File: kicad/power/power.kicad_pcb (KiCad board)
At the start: 2 copper layers, 73 x 25.1 mm, 45 parts, among them J1 Conn_01x06, J2 Conn_01x09_Male, U1 LF353DR, U2 LF353DR, U3 LF353DR, U4 LM339DR, U5 LM339DR

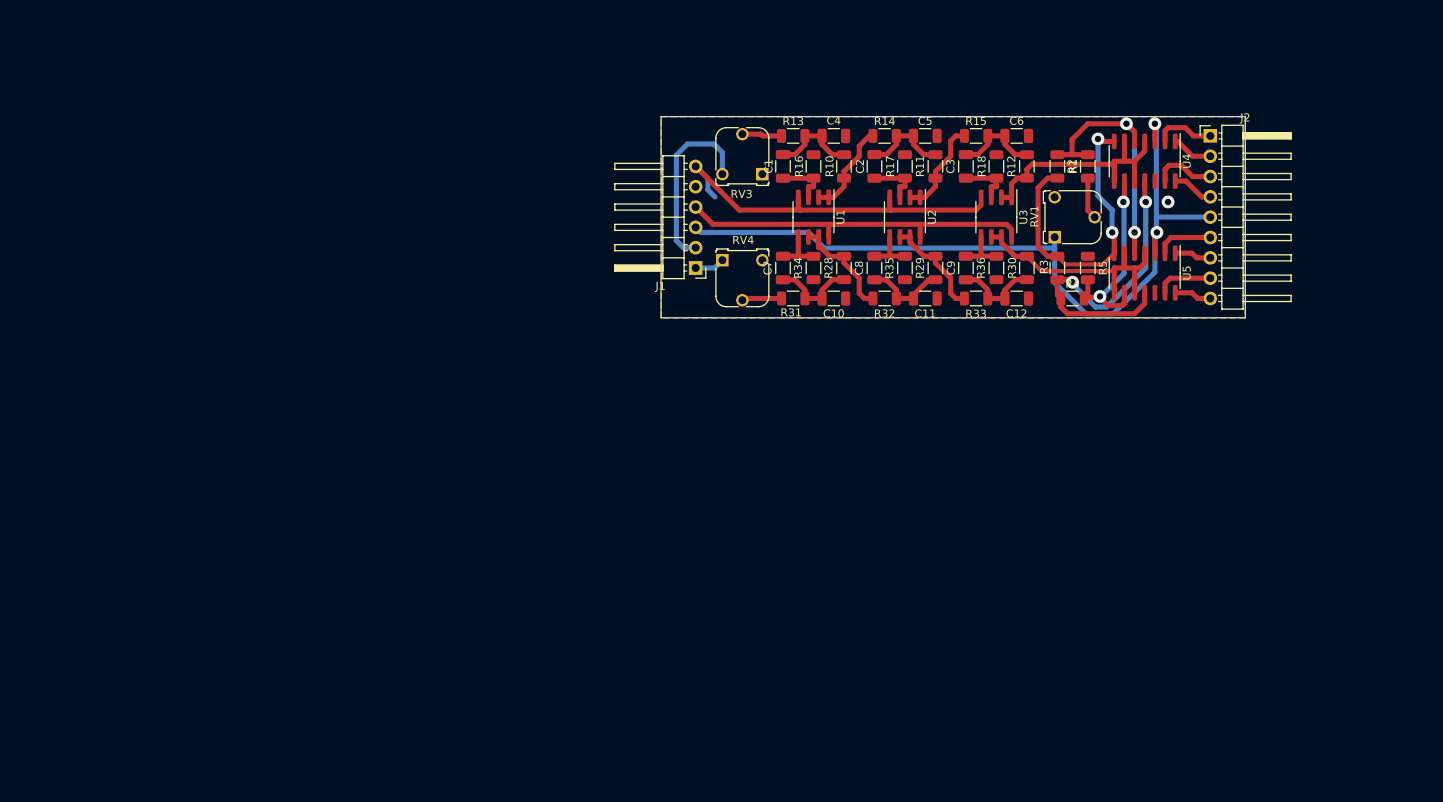
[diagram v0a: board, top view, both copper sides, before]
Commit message: Power schematic to pcb update
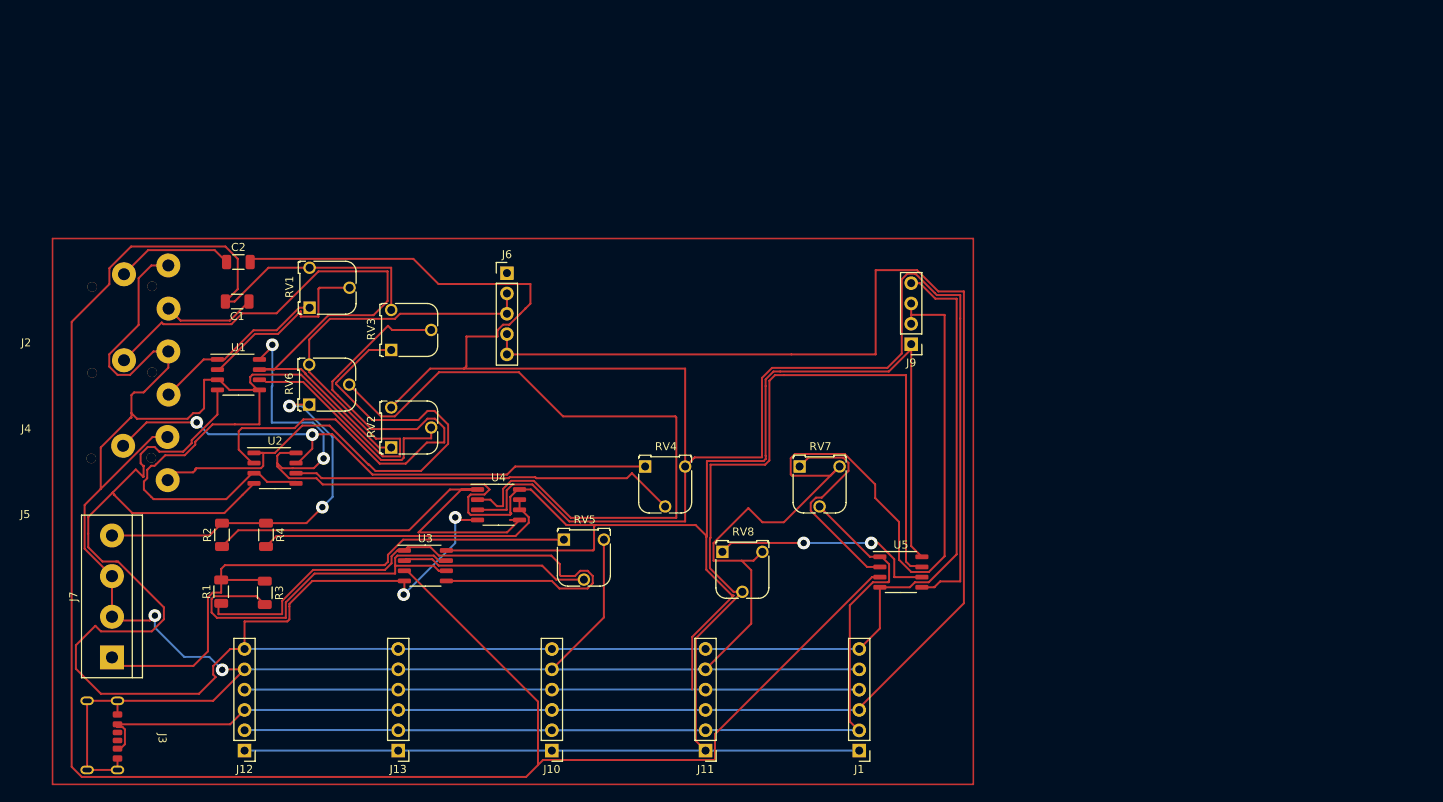
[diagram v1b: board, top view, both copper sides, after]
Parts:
- removed C10, C11, C12, C3, C4, C5, C6, C7, C8, C9: 100n, Capacitor_SMD:C_1206_3216Metric
- removed R10, R11, R12, R28, R29, R30: 137, Resistor_SMD:R_1206_3216Metric
- removed R13, R14, R15, R31, R32, R33: 931, Resistor_SMD:R_1206_3216Metric
- removed R16, R17, R18, R34, R35, R36: 1k87, Resistor_SMD:R_1206_3216Metric
- removed R5: 100k, Resistor_SMD:R_1206_3216Metric
- added J10: Conn_01x06, Connector_PinHeader_2.54mm:PinHeader_1x06_P2.54mm_Vertical, F.Cu at (103.2, 141.0)
- added J11: Conn_01x06, Connector_PinHeader_2.54mm:PinHeader_1x06_P2.54mm_Vertical, F.Cu at (122.4, 141.0)
- added J12: Conn_01x06, Connector_PinHeader_2.54mm:PinHeader_1x06_P2.54mm_Vertical, F.Cu at (64.8, 141.0)
- added J13: Conn_01x06, Connector_PinHeader_2.54mm:PinHeader_1x06_P2.54mm_Vertical, F.Cu at (84.0, 141.0)
- added J3: USB_C_Receptacle, audio_footprint:usb_footprint, F.Cu at (48.9, 139.4)
- added J4: AudioJack3, audio_footprint:audio_jack, F.Cu at (37.5, 101.2)
- added J5: AudioJack3, audio_footprint:audio_jack, F.Cu at (37.4, 111.9)
- added J6: Conn_01x05_Male, Connector_PinHeader_2.54mm:PinHeader_1x05_P2.54mm_Vertical, F.Cu at (97.6, 81.3)
- added J7: Screw_Terminal_01x02, TerminalBlock:TerminalBlock_bornier-4_P5.08mm, F.Cu at (48.2, 129.3)
- added J9: Conn_01x04_Male, Connector_PinHeader_2.54mm:PinHeader_1x04_P2.54mm_Vertical, F.Cu at (148.1, 90.2)
- added RV2: R_Potentiometer, Potentiometer_THT:Potentiometer_Runtron_RM-065_Vertical, F.Cu at (83.1, 103.1)
- added RV5: R_Potentiometer, Potentiometer_THT:Potentiometer_Runtron_RM-065_Vertical, F.Cu at (104.7, 114.6)
- added RV6: R_Potentiometer, Potentiometer_THT:Potentiometer_Runtron_RM-065_Vertical, F.Cu at (72.8, 97.7)
- added RV7: 2k2, Potentiometer_THT:Potentiometer_Runtron_RM-065_Vertical, F.Cu at (134.2, 105.5)
- added RV8: 2k2, Potentiometer_THT:Potentiometer_Runtron_RM-065_Vertical, F.Cu at (124.5, 116.1)
- C1, C2: value 100n -> C
- J1: footprint Connector_PinHeader_2.54mm:PinHeader_1x06_P2.54mm_Horizontal -> Connector_PinHeader_2.54mm:PinHeader_1x06_P2.54mm_Vertical
- J2: value Conn_01x09_Male -> AudioJack3; footprint Connector_PinHeader_2.54mm:PinHeader_1x09_P2.54mm_Horizontal -> audio_footprint:audio_jack
- R1, R2, R3, R4: value 100k -> 20
- RV1, RV3, RV4: value 10k -> R_Potentiometer
- U1, U2, U3: value LF353DR -> LM4565F-GE2; footprint Package_SO:SOIC-8_3.9x4.9mm_P1.27mm -> Package_SO:SOP-8_3.9x4.9mm_P1.27mm
- U4: value LM339DR -> LM4565F-GE2; footprint Package_SO:SO-14_3.9x8.65mm_P1.27mm -> Package_SO:SOP-8_3.9x4.9mm_P1.27mm
- U5: value LM339DR -> LF353DR; footprint Package_SO:SO-14_3.9x8.65mm_P1.27mm -> Package_SO:SOP-8_3.9x4.9mm_P1.27mm
- moved J2 150.4 mm to (37.5, 90.5)
- moved R1 120.7 mm to (61.9, 121.1)
- moved R2 114.1 mm to (62.0, 114.0), turned to 90 degrees
- moved R3 107.1 mm to (67.3, 121.2)
- moved R4 105.1 mm to (67.5, 114.0), turned to -90 degrees
- moved RV1 93.6 mm to (72.9, 85.6)
- moved U4 91.5 mm to (96.5, 110.2), turned to 0 degrees
- moved U2 84.8 mm to (68.6, 105.7), turned to 0 degrees
- moved U3 83.6 mm to (87.4, 117.9), turned to 0 degrees
- moved C2 80.4 mm to (64.0, 79.9), turned to 0 degrees
- moved U1 74.5 mm to (64.0, 94.0), turned to 0 degrees
- moved C1 70.3 mm to (63.9, 84.8), turned to 180 degrees
- moved J1 63.7 mm to (141.6, 141.0)
- moved RV3 51.3 mm to (83.1, 90.9), turned to 90 degrees
- moved U5 48.2 mm to (146.8, 118.7), turned to 0 degrees
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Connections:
- C1 pad 1: Net-(C4-Pad1) -> Net-(C1-Pad1)
- C1 pad 2: Net-(C1-Pad2) -> audio_in_L
- C2 pad 1: Net-(C5-Pad1) -> Net-(C2-Pad1)
- C2 pad 2: Net-(C2-Pad2) -> audio_in_R
- J1 pad 1: Net-(J1-Pad1) -> audio_right
- J1 pad 2: Net-(J1-Pad2) -> audio_lefT
- J2 pad 4: Net-(U4-Pad14) -> (no net)
- J2 pad 5: +5V -> (no net)
- R1 pad 2: Net-(R1-Pad2) -> speaker_left
- R2 pad 1: Net-(R1-Pad2) -> Net-(R2-Pad1)
- R2 pad 2: Net-(R2-Pad2) -> speaker_right
- R3 pad 1: Net-(R2-Pad2) -> speaker_left
- R4 pad 1: Net-(R3-Pad2) -> speaker_right
- RV1 pad 1: +5V -> Net-(J4-PadT)
- RV1 pad 2: Net-(R1-Pad1) -> Net-(RV1-Pad2)
- RV1 pad 3: GND -> audio_in_L
- RV3 pad 1: GND -> Net-(J5-PadT)
- RV3 pad 2: audio_left -> Net-(RV3-Pad2)
- RV3 pad 3: Net-(J1-Pad2) -> audio_in_L
- RV4 pad 1: Net-(J1-Pad1) -> Net-(J5-PadR)
- RV4 pad 2: audio_right -> Net-(RV4-Pad2)
- RV4 pad 3: GND -> audio_in_R
- U1 pad 1: Net-(R10-Pad2) -> Net-(J4-PadT)
- U1 pad 2: Net-(R10-Pad2) -> Net-(RV1-Pad2)
- U1 pad 3: Net-(C1-Pad2) -> GND
- U1 pad 5: Net-(C7-Pad2) -> GND
- U1 pad 6: Net-(R28-Pad2) -> Net-(RV2-Pad2)
- U1 pad 7: Net-(R28-Pad2) -> Net-(J4-PadR)
- U2 pad 1: Net-(R11-Pad2) -> Net-(J5-PadT)
- U2 pad 2: Net-(R11-Pad2) -> Net-(RV3-Pad2)
- U2 pad 3: Net-(C2-Pad2) -> GND
- U2 pad 5: Net-(C8-Pad2) -> GND
- U2 pad 6: Net-(R29-Pad2) -> Net-(RV4-Pad2)
- U2 pad 7: Net-(R29-Pad2) -> Net-(J5-PadR)
- U3 pad 1: Net-(R12-Pad2) -> Net-(R1-Pad1)
- U3 pad 2: Net-(R12-Pad2) -> Net-(RV5-Pad2)
- U3 pad 3: Net-(C3-Pad2) -> audio_in_L
- U3 pad 5: Net-(C9-Pad2) -> Net-(R1-Pad1)
- U3 pad 6: Net-(R30-Pad2) -> Net-(R3-Pad2)
- U3 pad 7: Net-(R30-Pad2) -> Net-(R3-Pad2)
- U4 pad 1: Net-(U4-Pad1) -> Net-(R2-Pad1)
- U4 pad 2: Net-(U4-Pad2) -> Net-(RV6-Pad2)
- U4 pad 3: +5V -> audio_in_R
- U4 pad 4: Net-(R12-Pad2) -> -15V
- U4 pad 5: Net-(R1-Pad2) -> Net-(R2-Pad1)
- U4 pad 6: Net-(R12-Pad2) -> Net-(R4-Pad2)
- U4 pad 7: Net-(R2-Pad2) -> Net-(R4-Pad2)
- U4 pad 8: Net-(R12-Pad2) -> +15V
- U5 pad 1: Net-(U5-Pad1) -> audio_lefT
- U5 pad 2: Net-(U5-Pad2) -> Net-(RV7-Pad1)
- U5 pad 3: +5V -> audio_in_L
- U5 pad 4: Net-(R30-Pad2) -> -15V
- U5 pad 5: Net-(R1-Pad2) -> audio_in_R
- U5 pad 6: Net-(R30-Pad2) -> Net-(RV8-Pad1)
- U5 pad 7: Net-(R2-Pad2) -> audio_right
- U5 pad 8: Net-(R30-Pad2) -> +15V
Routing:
- net GND: track 0.00 -> 492.8 mm, vias 1 -> 7
- net audio_in_L: track 0.00 -> 261.3 mm
- net +15V: track 44.8 -> 296.4 mm, vias 0 -> 7
- net -15V: track 46.4 -> 287.2 mm, vias 0 -> 7
- net audio_in_R: track 0.00 -> 239.6 mm
- net audio_right: track 4.98 -> 179.9 mm, vias 0 -> 4
- net +5V: track 98.4 -> 227.9 mm, vias 2 -> 5
- net audio_lefT: track 0.00 -> 113.0 mm, vias 0 -> 5
- net Net-(RV6-Pad2): track 0.00 -> 89.4 mm
- net Net-(J4-PadR): track 0.00 -> 81.6 mm
- net speaker_left: track 0.00 -> 75.2 mm
- net Net-(J5-PadR): track 0.00 -> 74.2 mm, vias 0 -> 2
- net Net-(J5-PadT): track 0.00 -> 73.2 mm
- net Net-(R1-Pad1): track 5.24 -> 76.0 mm
- net Net-(RV3-Pad2): track 0.00 -> 69.9 mm
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- removed copper zone on B.Cu, net GND
- removed copper zone on F.Cu, net GND
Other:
- board outline removed

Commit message: Did some stuff
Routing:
- net audio_in_R: track 239.6 -> 245.0 mm
- net -15V: track 287.2 -> 283.8 mm
- net GND: track 492.8 -> 491.9 mm
- added copper zone on B.Cu, net GND
- added copper zone on F.Cu, net GND
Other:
- board outline added: 115.3 x 68.1 mm

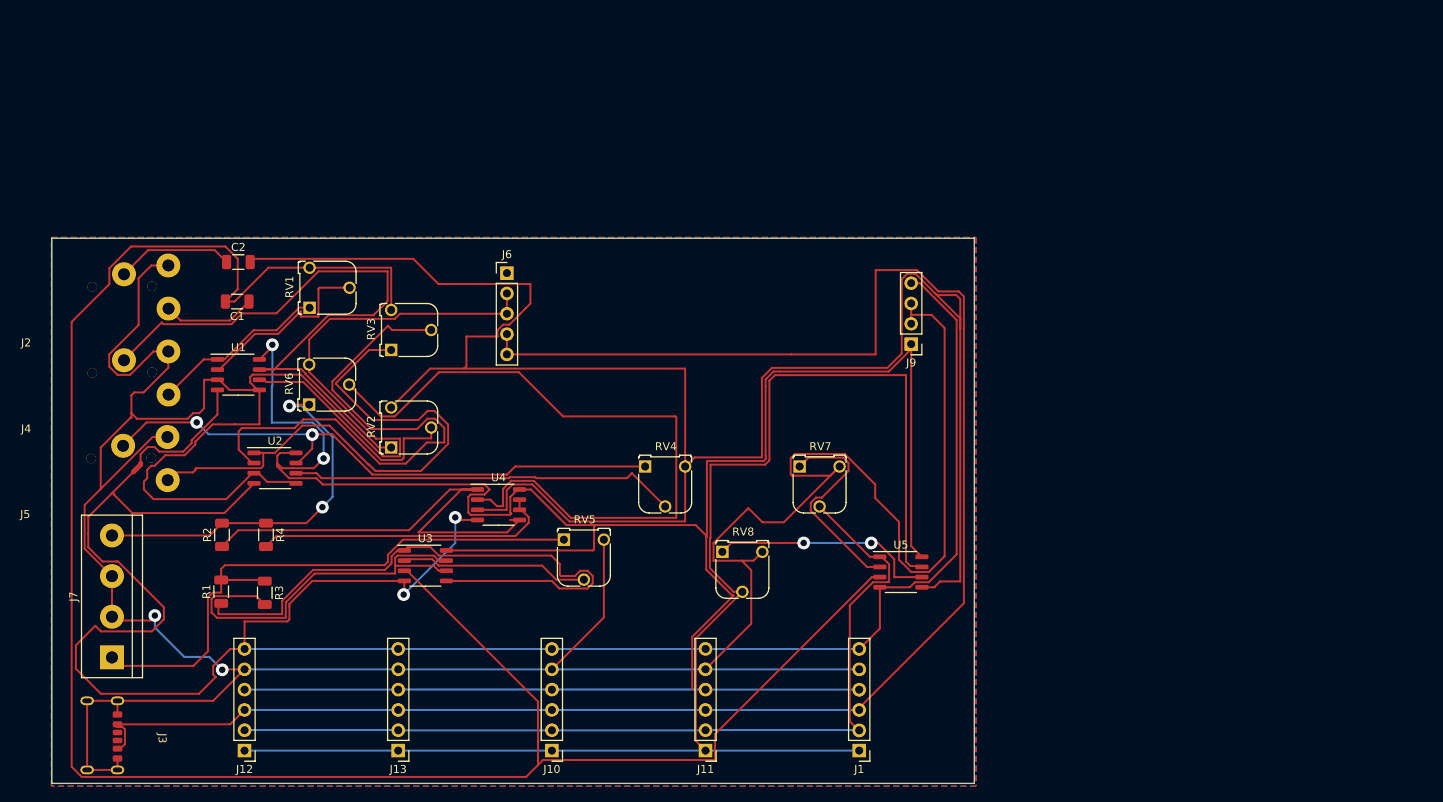
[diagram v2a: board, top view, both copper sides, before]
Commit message: Revision of PCB power circuit
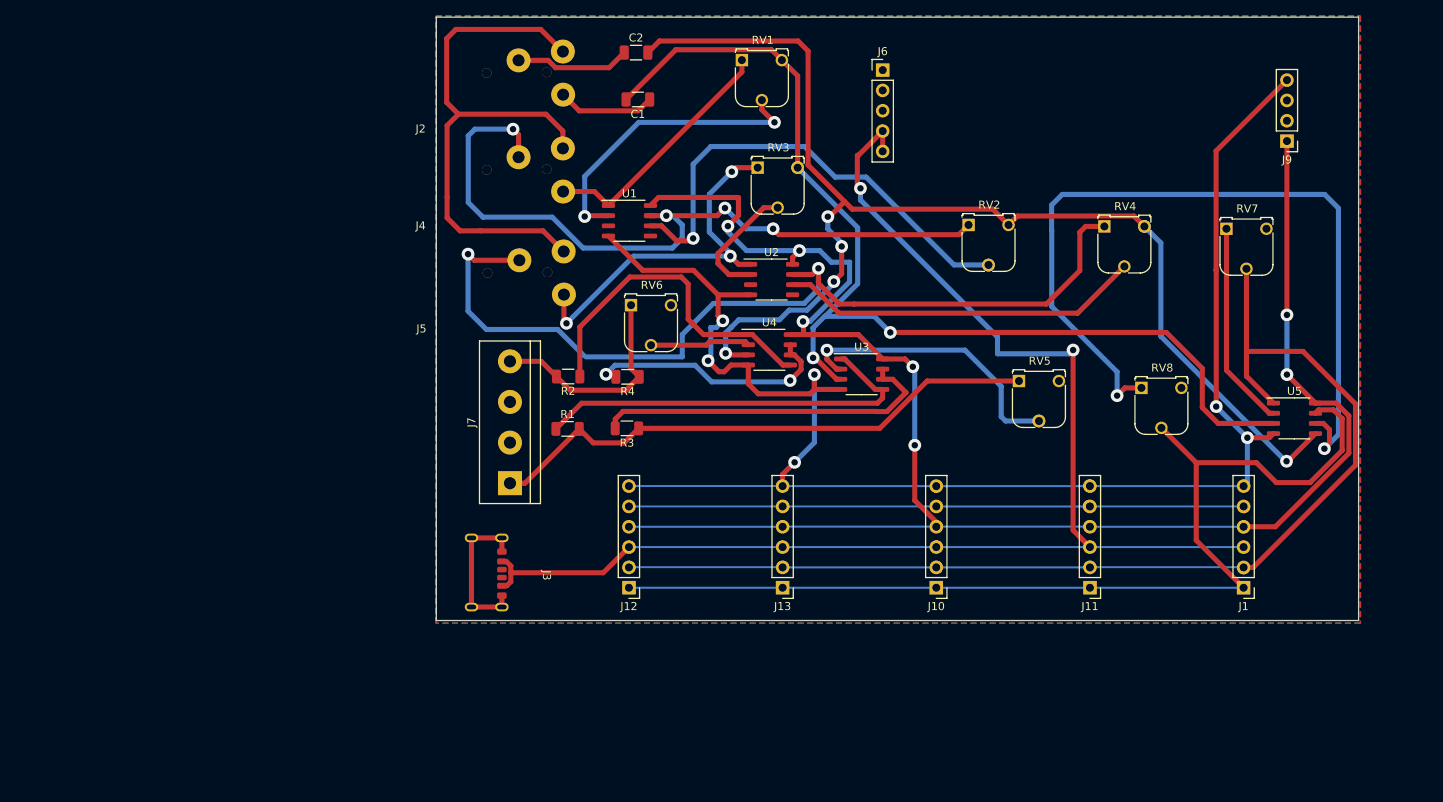
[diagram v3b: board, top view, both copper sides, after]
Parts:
- moved RV2 77.3 mm to (155.3, 75.3), turned to 0 degrees
- moved U2 66.4 mm to (130.7, 82.1)
- moved RV4 64.8 mm to (172.2, 75.5)
- moved RV1 62.3 mm to (126.9, 54.7), turned to 0 degrees
- moved RV7 61.1 mm to (187.5, 75.7)
- moved RV5 60.2 mm to (161.6, 94.8)
- moved U3 59.6 mm to (141.9, 93.9)
- moved RV8 56.2 mm to (176.9, 95.6)
- moved C2 56.2 mm to (113.7, 53.7)
- moved J2 56.1 mm to (86.8, 63.7)
- moved C1 56.1 mm to (113.9, 59.6)
- moved J4 55.5 mm to (86.8, 75.9)
- moved J5 54.7 mm to (86.9, 88.7)
- moved J7 54.3 mm to (98.0, 107.5)
- moved J6 53.4 mm to (144.5, 55.9)
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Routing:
- net GND: track 491.9 -> 168.3 mm, vias 7 -> 5
- net audio_in_L: track 261.3 -> 135.1 mm, vias 0 -> 3
- net audio_in_R: track 245.0 -> 157.2 mm, vias 0 -> 6
- net -15V: track 283.8 -> 204.5 mm, vias 7 -> 11
- net Net-(RV6-Pad2): track 89.4 -> 12.5 mm
- net Net-(RV8-Pad1): track 28.5 -> 103.3 mm
- net +15V: track 296.4 -> 222.8 mm, vias 7 -> 12
- net +5V: track 227.5 -> 171.8 mm, vias 5 -> 7
- net Net-(RV3-Pad2): track 69.9 -> 15.7 mm
- net audio_right: track 179.9 -> 130.0 mm
- net Net-(J5-PadR): track 74.2 -> 116.5 mm
- net Net-(RV2-Pad2): track 28.6 -> 59.5 mm, vias 0 -> 2
- net Net-(J5-PadT): track 73.2 -> 47.0 mm, vias 0 -> 3
- net Net-(R1-Pad1): track 76.0 -> 50.3 mm
- net audio_lefT: track 113.0 -> 138.4 mm
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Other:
- board size 115.3 x 68.1 mm -> 115.3 x 75.4 mm

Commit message: Power PCB revisions
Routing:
- net audio_right: track 130.0 -> 206.8 mm, vias 4 -> 0
- net +5V: track 171.8 -> 248.6 mm, vias 7 -> 2
- net +15V: track 222.8 -> 299.6 mm, vias 12 -> 7
- net GND: track 168.3 -> 245.1 mm, vias 5 -> 0
- net audio_lefT: track 138.4 -> 215.0 mm, vias 5 -> 0
- net -15V: track 204.5 -> 280.6 mm, vias 11 -> 5
- net Net-(J4-PadR): track 94.9 -> 69.5 mm, vias 4 -> 3
- net Net-(J5-PadR): track 116.5 -> 101.1 mm, vias 2 -> 1
- net Net-(RV1-Pad2): track 38.0 -> 25.2 mm, vias 2 -> 0
- net Net-(RV8-Pad1): track 103.3 -> 100.7 mm, vias 2 -> 1
- net audio_in_R: vias 6 -> 5
- net audio_in_L: vias 3 -> 2
- net Net-(RV5-Pad2): vias 2 -> 1
- net Net-(RV2-Pad2): vias 2 -> 1
- net Net-(J5-PadT): vias 3 -> 2

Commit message: Power Newest
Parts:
- moved RV7 6.77 mm to (187.5, 82.5)
- moved J6 6.13 mm to (139.5, 59.5)
- moved RV4 5.97 mm to (172.2, 81.4)
- moved J9 5.91 mm to (190.3, 68.3)
- moved RV2 5.91 mm to (154.8, 81.2)
- moved RV3 5.05 mm to (125.1, 64.8)
- moved RV1 2.86 mm to (124.1, 54.8)
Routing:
- net Net-(RV2-Pad2): track 59.5 -> 81.9 mm
- net audio_lefT: track 215.0 -> 208.3 mm
- net Net-(RV7-Pad1): track 25.8 -> 19.0 mm
- net -15V: track 280.6 -> 275.1 mm
- net Net-(J4-PadR): track 69.5 -> 73.5 mm
- net Net-(J5-PadT): track 47.0 -> 44.4 mm, vias 2 -> 1
- net audio_in_R: track 157.2 -> 159.5 mm
- net audio_in_L: track 135.1 -> 137.4 mm
- net Net-(J5-PadR): track 101.1 -> 99.2 mm
- net Net-(J4-PadT): track 31.5 -> 30.2 mm
- net +5V: track 248.6 -> 247.4 mm, vias 2 -> 1
- net +15V: track 299.6 -> 298.7 mm
- net Net-(RV3-Pad2): track 15.7 -> 16.5 mm

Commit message: Made some new stuffs
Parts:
- removed J5: AudioJack3, audio_footprint:audio_jack
- removed J7: Screw_Terminal_01x02, TerminalBlock:TerminalBlock_bornier-4_P5.08mm
- removed R3, R4: 20, Resistor_SMD:R_1206_3216Metric
- removed RV3, RV4, RV5, RV6: R_Potentiometer, Potentiometer_THT:Potentiometer_Runtron_RM-065_Vertical
- removed RV7, RV8: 2k2, Potentiometer_THT:Potentiometer_Runtron_RM-065_Vertical
- removed U2, U3, U4: LM4565F-GE2, Package_SO:SOP-8_3.9x4.9mm_P1.27mm
- C1, C2: value C -> 1u
- R1, R2: value 20 -> 100k
- RV1, RV2: value R_Potentiometer -> R_Potentiometer_Dual_Separate; footprint Potentiometer_THT:Potentiometer_Runtron_RM-065_Vertical -> Potentiometer_THT:Potentiometer_Alpha_RD902F-40-00D_Dual_Vertical
- moved RV1 48.8 mm to (97.8, 95.8), turned to 180 degrees
- moved RV2 46.2 mm to (200.0, 90.8)
- moved J4 31.4 mm to (95.2, 106.0)
- moved C2 30.0 mm to (108.0, 83.2)
- moved J6 25.6 mm to (130.0, 83.2)
- moved J9 25.6 mm to (180.8, 92.1)
- moved R1 24.2 mm to (113.7, 78.1)
- moved C1 19.5 mm to (108.0, 78.1), turned to 0 degrees
- moved J2 18.9 mm to (95.2, 80.6)
- moved U1 17.3 mm to (113.0, 92.1)
- moved R2 13.9 mm to (113.7, 83.2), turned to 0 degrees
- moved U5 8.32 mm to (189.2, 94.6), turned to 180 degrees
- moved J10 4.72 mm to (149.3, 116.3)
- moved J11 4.72 mm to (168.5, 116.3)
- moved J13 4.72 mm to (130.1, 116.3)
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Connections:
- J6 pad 1: -5V -> unconnected-(J6-Pad1)
- J9 pad 1: +15V -> -15V
- J9 pad 4: -15V -> +15V
- R1 pad 1: Net-(R1-Pad1) -> audio_in_L
- R1 pad 2: speaker_left -> GND
- R2 pad 1: Net-(R2-Pad1) -> audio_in_R
- R2 pad 2: speaker_right -> GND
- RV1 pad 1: Net-(J4-PadT) -> Net-(U1-Pad2)
- RV1 pad 2: Net-(RV1-Pad2) -> Net-(J4-PadT)
- RV1 pad 3: audio_in_L -> GND
- RV2 pad 1: Net-(J4-PadR) -> Net-(U5-Pad2)
- RV2 pad 2: Net-(RV2-Pad2) -> audio_lefT
- RV2 pad 3: audio_in_R -> GND
- U1 pad 2: Net-(RV1-Pad2) -> Net-(U1-Pad2)
- U1 pad 3: GND -> audio_in_L
- U1 pad 5: GND -> audio_in_R
- U1 pad 6: Net-(RV2-Pad2) -> Net-(U1-Pad6)
- U5 pad 2: Net-(RV7-Pad1) -> Net-(U5-Pad2)
- U5 pad 6: Net-(RV8-Pad1) -> Net-(U5-Pad6)
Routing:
- net audio_in_R: track 159.5 -> 15.8 mm, vias 5 -> 0
- net audio_in_L: track 137.4 -> 23.3 mm, vias 2 -> 0
- net Net-(RV8-Pad1): track 100.7 -> 0.00 mm, vias 1 -> 0
- net Net-(J5-PadR): track 99.2 -> 0.00 mm, vias 1 -> 0
- net -15V: track 275.1 -> 177.1 mm, vias 5 -> 1
- net Net-(RV2-Pad2): track 81.9 -> 0.00 mm, vias 1 -> 0
- net GND: track 245.1 -> 172.9 mm
- net speaker_left: track 70.4 -> 0.00 mm
- net Net-(R1-Pad1): track 50.3 -> 0.00 mm
- net Net-(RV4-Pad2): track 45.2 -> 0.00 mm
- net Net-(J5-PadT): track 44.4 -> 0.00 mm, vias 1 -> 0
- net Net-(R3-Pad2): track 43.8 -> 0.00 mm
- net Net-(R2-Pad1): track 42.2 -> 0.00 mm
- net audio_right: track 206.8 -> 168.6 mm, vias 0 -> 1
- net Net-(RV5-Pad2): track 35.8 -> 0.00 mm, vias 1 -> 0
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- removed copper zone on B.Cu, net GND
- removed copper zone on F.Cu, net GND
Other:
- board size 115.3 x 75.4 mm -> 114.9 x 75.4 mm
